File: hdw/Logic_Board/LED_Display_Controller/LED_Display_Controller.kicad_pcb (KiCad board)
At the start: 4 copper layers, 855 parts, among them J1101 USB_B_Mini, J1401 Encoder Ext, J1601 POS5P EXT, J1602 POS5P PGOOD, J1603 POS5P_THWN, J1604 POS5P_RUN, J201 +12V IN, J202 GND IN, J203 +12V IN AUX, J204 Master Power SW, J2901 STRING 1, J2902 STRING 2, J2903 STRING 3, J2904 STRING 4, J3001 USB UART, J3002 WIFI UART, J3003 FLASH SPI, J3004 Panel TP, J501 PICKIT3, J901 ESP8266 Socket, Q201 IPC100N04S51R7ATMA1, Q202 IPC100N04S51R7ATMA1, Q501 BSS214NW, Q901 BSS214NW, SW1401 Display Enable, SW1402 Brightness/Enable, SW501 MRST, U1001 ISO7321C, U1101 LT6700-1-S6, U1102 FT234XD, U1103 74LVC1G06, U1104 TPD3S014DBVR, U1201 74LVC1G06, U1202 74LVC1G06, U1203 74LVC1G06, U1204 74LVC1G06, U1205 74LVC1G06, U1206 74LVC1G06, U1207 74LVC1G06, U1301 74LVC1G06, U1302 74LVC1G06, U1303 74LVC1G06, U1304 74LVC1G06, U1401 MAX6816, U1402 74LVC2G14, U1403 74LVC1G79, U1601 LM1117-ADJ, U1602 NUP2202, U1603 74LVC1G17, U1604 74LVC1G17, U1605 74LVC1G17, U1606 NUP2202, U1701 CY7C1010DV33, U1801 SST25PF020B, U1901 SST25PF020B, U2001 SST25PF020B, U201 LTC4365DDB, U2101 SST25PF020B, U2201 SST25PF020B, U2301 SST25PF020B, U2401 SST25PF020B, U2501 SST25PF020B, U2601 74HCT541, U2602 74HCT541, U2701 74HCT541, U2702 74HCT541, U2801 74LVC1G32, U2802 74HCT541, U301 LTC3605A_UF, U401 LTC3624DD, U601 PIC32MZ2048EFH144_IPL

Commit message: Arranged USB, routed EBI
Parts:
- removed the C1801 at (123.3, 175.6)
- removed the C1801 at (123.3, 168.6)
- removed the C1801 at (123.3, 161.6)
- removed the C1801 at (123.3, 154.6)
- removed the C1801 at (123.3, 147.6)
- removed the C1801 at (123.3, 140.6)
- removed the C1801 at (123.3, 133.6)
- removed the C1802 at (123.3, 177.0)
- removed the C1802 at (123.3, 170.0)
- removed the C1802 at (123.3, 163.0)
- removed the C1802 at (123.3, 156.0)
- removed the C1802 at (123.3, 149.0)
- removed the C1802 at (123.3, 142.0)
- removed the C1802 at (123.3, 135.0)
- removed the C1803 at (123.3, 178.4)
- removed the C1803 at (123.3, 171.4)
- removed the C1803 at (123.3, 164.4)
- removed the C1803 at (123.3, 157.4)
- removed the C1803 at (123.3, 150.4)
- removed the C1803 at (123.3, 143.4)
- removed the C1803 at (123.3, 136.4)
- removed the R1801 at (130.3, 179.0)
- removed the R1801 at (130.3, 172.0)
- removed the R1801 at (130.3, 165.0)
- removed the R1801 at (130.3, 158.0)
- removed the R1801 at (130.3, 151.0)
- removed the R1801 at (130.3, 144.0)
- removed the R1801 at (130.3, 137.0)
- removed the R1802 at (130.3, 176.3)
- removed the R1802 at (130.3, 169.3)
- removed the R1802 at (130.3, 162.3)
- removed the R1802 at (130.3, 155.3)
- removed the R1802 at (130.3, 148.3)
- removed the R1802 at (130.3, 141.3)
- removed the R1802 at (130.3, 134.3)
- removed the R1803 at (116.3, 177.8)
- removed the R1803 at (116.3, 170.8)
- removed the R1803 at (116.3, 163.8)
- removed the R1803 at (116.3, 156.8)
- removed the R1803 at (116.3, 149.8)
- removed the R1803 at (116.3, 142.8)
- removed the R1803 at (116.3, 135.8)
- removed the R1804 at (116.3, 175.0)
- removed the R1804 at (116.3, 168.0)
- removed the R1804 at (116.3, 161.0)
- removed the R1804 at (116.3, 154.0)
- removed the R1804 at (116.3, 147.0)
- removed the R1804 at (116.3, 140.0)
- removed the R1804 at (116.3, 133.0)
- removed the R1805 at (130.3, 177.7)
- removed the R1805 at (130.3, 170.7)
- removed the R1805 at (130.3, 163.7)
- removed the R1805 at (130.3, 156.7)
- removed the R1805 at (130.3, 149.7)
- removed the R1805 at (130.3, 142.7)
- removed the R1805 at (130.3, 135.7)
- removed the R1806 at (116.3, 177.8)
- removed the R1806 at (116.3, 170.8)
- removed the R1806 at (116.3, 163.8)
- removed the R1806 at (116.3, 156.8)
- removed the R1806 at (116.3, 149.8)
- removed the R1806 at (116.3, 142.8)
- removed the R1806 at (116.3, 135.8)
- removed the R1807 at (116.3, 175.0)
- removed the R1807 at (116.3, 168.0)
- removed the R1807 at (116.3, 161.0)
- removed the R1807 at (116.3, 154.0)
- removed the R1807 at (116.3, 147.0)
- removed the R1807 at (116.3, 140.0)
- removed the R1807 at (116.3, 133.0)
- removed the R1808 at (130.3, 177.7)
- removed the R1808 at (130.3, 170.7)
- removed the R1808 at (130.3, 163.7)
- removed the R1808 at (130.3, 156.7)
- removed the R1808 at (130.3, 149.7)
- removed the R1808 at (130.3, 142.7)
- removed the R1808 at (130.3, 135.7)
- removed the R1809 at (130.3, 176.3)
- removed the R1809 at (130.3, 169.3)
- removed the R1809 at (130.3, 162.3)
- removed the R1809 at (130.3, 155.3)
- removed the R1809 at (130.3, 148.3)
- removed the R1809 at (130.3, 141.3)
- removed the R1809 at (130.3, 134.3)
- removed the R1810 at (130.3, 179.0)
- removed the R1810 at (130.3, 172.0)
- removed the R1810 at (130.3, 165.0)
- removed the R1810 at (130.3, 158.0)
- removed the R1810 at (130.3, 151.0)
- removed the R1810 at (130.3, 144.0)
- removed the R1810 at (130.3, 137.0)
- removed the R1811 at (116.3, 176.4)
- removed the R1811 at (116.3, 169.4)
- removed the R1811 at (116.3, 162.4)
- removed the R1811 at (116.3, 155.4)
- removed the R1811 at (116.3, 148.4)
- removed the R1811 at (116.3, 141.4)
- removed the R1811 at (116.3, 134.4)
- removed the R1812 at (116.3, 176.4)
- removed the R1812 at (116.3, 169.4)
- removed the R1812 at (116.3, 162.4)
- removed the R1812 at (116.3, 155.4)
- removed the R1812 at (116.3, 148.4)
- removed the R1812 at (116.3, 141.4)
- removed the R1812 at (116.3, 134.4)
- removed the R2601 at (121.8, 93.4)
- removed the R2601 at (121.8, 78.4)
- removed the R2601 at (121.8, 63.4)
- removed the R2601 at (121.8, 48.4)
- removed the R2602 at (121.8, 94.8)
- removed the R2602 at (121.8, 79.8)
- removed the R2602 at (121.8, 64.8)
- removed the R2602 at (121.8, 49.8)
- removed the R2603 at (121.8, 96.2)
- removed the R2603 at (121.8, 81.2)
- removed the R2603 at (121.8, 66.2)
- removed the R2603 at (121.8, 51.2)
- removed the R2604 at (121.8, 97.6)
- removed the R2604 at (121.8, 82.6)
- removed the R2604 at (121.8, 67.6)
- removed the R2604 at (121.8, 52.6)
- removed the R2605 at (121.8, 99.0)
- removed the R2605 at (121.8, 84.0)
- removed the R2605 at (121.8, 69.0)
- removed the R2605 at (121.8, 54.0)
- removed the R2606 at (121.8, 100.4)
- removed the R2606 at (121.8, 85.4)
- removed the R2606 at (121.8, 70.4)
- removed the R2606 at (121.8, 55.4)
- removed the R2615 at (121.8, 93.4)
- removed the R2615 at (121.8, 78.4)
- removed the R2615 at (121.8, 63.4)
- removed the R2615 at (121.8, 48.4)
- removed the R2617 at (121.8, 94.8)
- removed the R2617 at (121.8, 79.8)
- removed the R2617 at (121.8, 64.8)
- removed the R2617 at (121.8, 49.8)
- removed the R2619 at (121.8, 96.2)
- removed the R2619 at (121.8, 81.2)
- removed the R2619 at (121.8, 66.2)
- removed the R2619 at (121.8, 51.2)
- removed the R2621 at (121.8, 97.6)
- removed the R2621 at (121.8, 82.6)
- removed the R2621 at (121.8, 67.6)
- removed the R2621 at (121.8, 52.6)
- removed the R2623 at (121.8, 99.0)
- removed the R2623 at (121.8, 84.0)
- removed the R2623 at (121.8, 69.0)
- removed the R2623 at (121.8, 54.0)
- removed the R2625 at (121.8, 100.4)
- removed the R2625 at (121.8, 85.4)
- removed the R2625 at (121.8, 70.4)
- removed the R2625 at (121.8, 55.4)
- removed the R2627 at (121.8, 101.8)
- removed the R2627 at (121.8, 86.8)
- removed the R2627 at (121.8, 71.8)
- removed the R2627 at (121.8, 56.8)
- removed the R2629 at (121.8, 103.2)
- removed the R2629 at (121.8, 88.2)
- removed the R2629 at (121.8, 73.2)
- removed the R2629 at (121.8, 58.2)
- removed the R2631 at (136.0, 94.8)
- removed the R2631 at (136.0, 79.8)
- removed the R2631 at (136.0, 64.8)
- removed the R2631 at (136.0, 49.8)
- removed the R2633 at (136.0, 96.2)
- removed the R2633 at (136.0, 81.2)
- removed the R2633 at (136.0, 66.2)
- removed the R2633 at (136.0, 51.2)
- removed the R2635 at (136.0, 97.6)
- removed the R2635 at (136.0, 82.6)
- removed the R2635 at (136.0, 67.6)
- removed the R2635 at (136.0, 52.6)
- removed the R2637 at (136.0, 99.0)
- removed the R2637 at (136.0, 84.0)
- removed the R2637 at (136.0, 69.0)
- removed the R2637 at (136.0, 54.0)
- removed the R2639 at (136.0, 100.4)
- removed the R2639 at (136.0, 85.4)
- removed the R2639 at (136.0, 70.4)
- removed the R2639 at (136.0, 55.4)
- removed the R2641 at (136.0, 101.8)
- removed the R2641 at (136.0, 86.8)
- removed the R2641 at (136.0, 71.8)
- removed the R2641 at (136.0, 56.8)
- removed the R2643 at (136.0, 94.8)
- removed the R2643 at (136.0, 79.8)
- removed the R2643 at (136.0, 64.8)
- removed the R2643 at (136.0, 49.8)
- removed the R2644 at (136.0, 96.2)
- removed the R2644 at (136.0, 81.2)
- removed the R2644 at (136.0, 66.2)
- removed the R2644 at (136.0, 51.2)
- removed the R2645 at (136.0, 97.6)
- removed the R2645 at (136.0, 82.6)
- removed the R2645 at (136.0, 67.6)
- removed the R2645 at (136.0, 52.6)
- removed the R2646 at (136.0, 99.0)
- removed the R2646 at (136.0, 84.0)
- removed the R2646 at (136.0, 69.0)
- removed the R2646 at (136.0, 54.0)
- removed the R2647 at (136.0, 100.4)
- removed the R2647 at (136.0, 85.4)
- removed the R2647 at (136.0, 70.4)
- removed the R2647 at (136.0, 55.4)
- removed the R2648 at (136.0, 101.8)
- removed the R2648 at (136.0, 86.8)
- removed the R2648 at (136.0, 71.8)
- removed the R2648 at (136.0, 56.8)
- removed the U1801 at (123.3, 177.0)
- removed the U1801 at (123.3, 170.0)
- removed the U1801 at (123.3, 163.0)
- removed the U1801 at (123.3, 156.0)
- removed the U1801 at (123.3, 149.0)
- removed the U1801 at (123.3, 142.0)
- removed the U1801 at (123.3, 135.0)
- added C1801: 0.1uF, Capacitors_SMD:C_0603, B.Cu at (123.3, 182.6)
- added C1801: 0.1uF, Capacitors_SMD:C_0603, B.Cu at (123.3, 174.6)
- added C1801: 0.1uF, Capacitors_SMD:C_0603, B.Cu at (123.3, 166.6)
- added C1801: 0.1uF, Capacitors_SMD:C_0603, B.Cu at (123.3, 158.6)
- added C1801: 0.1uF, Capacitors_SMD:C_0603, B.Cu at (123.3, 150.6)
- added C1801: 0.1uF, Capacitors_SMD:C_0603, B.Cu at (123.3, 142.6)
- added C1801: 0.1uF, Capacitors_SMD:C_0603, B.Cu at (123.3, 134.6)
- added C1802: 10nF, Capacitors_SMD:C_0603, B.Cu at (123.3, 184.0)
- added C1802: 10nF, Capacitors_SMD:C_0603, B.Cu at (123.3, 176.0)
- added C1802: 10nF, Capacitors_SMD:C_0603, B.Cu at (123.3, 168.0)
- added C1802: 10nF, Capacitors_SMD:C_0603, B.Cu at (123.3, 160.0)
- added C1802: 10nF, Capacitors_SMD:C_0603, B.Cu at (123.3, 152.0)
- added C1802: 10nF, Capacitors_SMD:C_0603, B.Cu at (123.3, 144.0)
- added C1802: 10nF, Capacitors_SMD:C_0603, B.Cu at (123.3, 136.0)
- added C1803: 1nF, Capacitors_SMD:C_0603, B.Cu at (123.3, 185.4)
- added C1803: 1nF, Capacitors_SMD:C_0603, B.Cu at (123.3, 177.4)
- added C1803: 1nF, Capacitors_SMD:C_0603, B.Cu at (123.3, 169.4)
- added C1803: 1nF, Capacitors_SMD:C_0603, B.Cu at (123.3, 161.4)
- added C1803: 1nF, Capacitors_SMD:C_0603, B.Cu at (123.3, 153.4)
- added C1803: 1nF, Capacitors_SMD:C_0603, B.Cu at (123.3, 145.4)
- added C1803: 1nF, Capacitors_SMD:C_0603, B.Cu at (123.3, 137.4)
- added R1801: 100, Resistors_SMD:R_0603, F.Cu at (130.3, 186.2)
- added R1801: 100, Resistors_SMD:R_0603, F.Cu at (130.3, 178.2)
- added R1801: 100, Resistors_SMD:R_0603, F.Cu at (130.3, 170.2)
- added R1801: 100, Resistors_SMD:R_0603, F.Cu at (130.3, 162.2)
- added R1801: 100, Resistors_SMD:R_0603, F.Cu at (130.3, 154.2)
- added R1801: 100, Resistors_SMD:R_0603, F.Cu at (130.3, 146.2)
- added R1801: 100, Resistors_SMD:R_0603, F.Cu at (130.3, 138.2)
- added R1802: 100, Resistors_SMD:R_0603, F.Cu at (130.3, 183.1)
- added R1802: 100, Resistors_SMD:R_0603, F.Cu at (130.3, 175.1)
- added R1802: 100, Resistors_SMD:R_0603, F.Cu at (130.3, 167.1)
- added R1802: 100, Resistors_SMD:R_0603, F.Cu at (130.3, 159.1)
- added R1802: 100, Resistors_SMD:R_0603, F.Cu at (130.3, 151.1)
- added R1802: 100, Resistors_SMD:R_0603, F.Cu at (130.3, 143.1)
- added R1802: 100, Resistors_SMD:R_0603, F.Cu at (130.3, 135.1)
- added R1803: 100, Resistors_SMD:R_0603, F.Cu at (116.3, 184.9)
- added R1803: 100, Resistors_SMD:R_0603, F.Cu at (116.3, 176.9)
- added R1803: 100, Resistors_SMD:R_0603, F.Cu at (116.3, 168.9)
- added R1803: 100, Resistors_SMD:R_0603, F.Cu at (116.3, 160.9)
- added R1803: 100, Resistors_SMD:R_0603, F.Cu at (116.3, 152.9)
- added R1803: 100, Resistors_SMD:R_0603, F.Cu at (116.3, 144.9)
- added R1803: 100, Resistors_SMD:R_0603, F.Cu at (116.3, 136.9)
- added R1804: 100, Resistors_SMD:R_0603, F.Cu at (116.3, 181.9)
- added R1804: 100, Resistors_SMD:R_0603, F.Cu at (116.3, 173.9)
- added R1804: 100, Resistors_SMD:R_0603, F.Cu at (116.3, 165.9)
- added R1804: 100, Resistors_SMD:R_0603, F.Cu at (116.3, 157.9)
- added R1804: 100, Resistors_SMD:R_0603, F.Cu at (116.3, 149.9)
- added R1804: 100, Resistors_SMD:R_0603, F.Cu at (116.3, 141.9)
- added R1804: 100, Resistors_SMD:R_0603, F.Cu at (116.3, 133.9)
- added R1805: 100, Resistors_SMD:R_0603, F.Cu at (130.3, 184.7)
- added R1805: 100, Resistors_SMD:R_0603, F.Cu at (130.3, 176.7)
- added R1805: 100, Resistors_SMD:R_0603, F.Cu at (130.3, 168.7)
- added R1805: 100, Resistors_SMD:R_0603, F.Cu at (130.3, 160.7)
- added R1805: 100, Resistors_SMD:R_0603, F.Cu at (130.3, 152.7)
- added R1805: 100, Resistors_SMD:R_0603, F.Cu at (130.3, 144.7)
- added R1805: 100, Resistors_SMD:R_0603, F.Cu at (130.3, 136.7)
- added R1806: 10k, Resistors_SMD:R_0603, B.Cu at (116.3, 184.9)
- added R1806: 10k, Resistors_SMD:R_0603, B.Cu at (116.3, 176.9)
- added R1806: 10k, Resistors_SMD:R_0603, B.Cu at (116.3, 168.9)
- added R1806: 10k, Resistors_SMD:R_0603, B.Cu at (116.3, 160.9)
- added R1806: 10k, Resistors_SMD:R_0603, B.Cu at (116.3, 152.9)
- added R1806: 10k, Resistors_SMD:R_0603, B.Cu at (116.3, 144.9)
- added R1806: 10k, Resistors_SMD:R_0603, B.Cu at (116.3, 136.9)
- added R1807: 10k, Resistors_SMD:R_0603, B.Cu at (116.3, 181.9)
- added R1807: 10k, Resistors_SMD:R_0603, B.Cu at (116.3, 173.9)
- added R1807: 10k, Resistors_SMD:R_0603, B.Cu at (116.3, 165.9)
- added R1807: 10k, Resistors_SMD:R_0603, B.Cu at (116.3, 157.9)
- added R1807: 10k, Resistors_SMD:R_0603, B.Cu at (116.3, 149.9)
- added R1807: 10k, Resistors_SMD:R_0603, B.Cu at (116.3, 141.9)
- added R1807: 10k, Resistors_SMD:R_0603, B.Cu at (116.3, 133.9)
- added R1808: 10k, Resistors_SMD:R_0603, B.Cu at (130.3, 184.7)
- added R1808: 10k, Resistors_SMD:R_0603, B.Cu at (130.3, 176.7)
- added R1808: 10k, Resistors_SMD:R_0603, B.Cu at (130.3, 168.7)
- added R1808: 10k, Resistors_SMD:R_0603, B.Cu at (130.3, 160.7)
- added R1808: 10k, Resistors_SMD:R_0603, B.Cu at (130.3, 152.7)
- added R1808: 10k, Resistors_SMD:R_0603, B.Cu at (130.3, 144.7)
- added R1808: 10k, Resistors_SMD:R_0603, B.Cu at (130.3, 136.7)
- added R1809: 10k, Resistors_SMD:R_0603, B.Cu at (130.3, 183.1)
- added R1809: 10k, Resistors_SMD:R_0603, B.Cu at (130.3, 175.1)
- added R1809: 10k, Resistors_SMD:R_0603, B.Cu at (130.3, 167.1)
- added R1809: 10k, Resistors_SMD:R_0603, B.Cu at (130.3, 159.1)
- added R1809: 10k, Resistors_SMD:R_0603, B.Cu at (130.3, 151.1)
- added R1809: 10k, Resistors_SMD:R_0603, B.Cu at (130.3, 143.1)
- added R1809: 10k, Resistors_SMD:R_0603, B.Cu at (130.3, 135.1)
- added R1810: 10k, Resistors_SMD:R_0603, B.Cu at (130.3, 186.2)
- added R1810: 10k, Resistors_SMD:R_0603, B.Cu at (130.3, 178.2)
- added R1810: 10k, Resistors_SMD:R_0603, B.Cu at (130.3, 170.2)
- added R1810: 10k, Resistors_SMD:R_0603, B.Cu at (130.3, 162.2)
- added R1810: 10k, Resistors_SMD:R_0603, B.Cu at (130.3, 154.2)
- added R1810: 10k, Resistors_SMD:R_0603, B.Cu at (130.3, 146.2)
- added R1810: 10k, Resistors_SMD:R_0603, B.Cu at (130.3, 138.2)
- added R1811: 10k, Resistors_SMD:R_0603, B.Cu at (116.3, 183.4)
- added R1811: 10k, Resistors_SMD:R_0603, B.Cu at (116.3, 175.4)
- added R1811: 10k, Resistors_SMD:R_0603, B.Cu at (116.3, 167.4)
- added R1811: 10k, Resistors_SMD:R_0603, B.Cu at (116.3, 159.4)
- added R1811: 10k, Resistors_SMD:R_0603, B.Cu at (116.3, 151.4)
- added R1811: 10k, Resistors_SMD:R_0603, B.Cu at (116.3, 143.4)
- added R1811: 10k, Resistors_SMD:R_0603, B.Cu at (116.3, 135.4)
- added R1812: 100, Resistors_SMD:R_0603, F.Cu at (116.3, 183.4)
- added R1812: 100, Resistors_SMD:R_0603, F.Cu at (116.3, 175.4)
- added R1812: 100, Resistors_SMD:R_0603, F.Cu at (116.3, 167.4)
- added R1812: 100, Resistors_SMD:R_0603, F.Cu at (116.3, 159.4)
- added R1812: 100, Resistors_SMD:R_0603, F.Cu at (116.3, 151.4)
- added R1812: 100, Resistors_SMD:R_0603, F.Cu at (116.3, 143.4)
- added R1812: 100, Resistors_SMD:R_0603, F.Cu at (116.3, 135.4)
- added R2601: 100, Resistors_SMD:R_0603, F.Cu at (121.5, 93.0)
- added R2601: 100, Resistors_SMD:R_0603, F.Cu at (121.5, 78.0)
- added R2601: 100, Resistors_SMD:R_0603, F.Cu at (121.5, 63.0)
- added R2601: 100, Resistors_SMD:R_0603, F.Cu at (121.5, 48.0)
- added R2602: 100, Resistors_SMD:R_0603, F.Cu at (121.5, 94.5)
- added R2602: 100, Resistors_SMD:R_0603, F.Cu at (121.5, 79.5)
- added R2602: 100, Resistors_SMD:R_0603, F.Cu at (121.5, 64.5)
- added R2602: 100, Resistors_SMD:R_0603, F.Cu at (121.5, 49.5)
- added R2603: 100, Resistors_SMD:R_0603, F.Cu at (121.5, 96.1)
- added R2603: 100, Resistors_SMD:R_0603, F.Cu at (121.5, 81.1)
- added R2603: 100, Resistors_SMD:R_0603, F.Cu at (121.5, 66.1)
- added R2603: 100, Resistors_SMD:R_0603, F.Cu at (121.5, 51.1)
- added R2604: 100, Resistors_SMD:R_0603, F.Cu at (121.5, 97.6)
- added R2604: 100, Resistors_SMD:R_0603, F.Cu at (121.5, 82.6)
- added R2604: 100, Resistors_SMD:R_0603, F.Cu at (121.5, 67.6)
- added R2604: 100, Resistors_SMD:R_0603, F.Cu at (121.5, 52.6)
- added R2605: 100, Resistors_SMD:R_0603, F.Cu at (121.5, 99.1)
- added R2605: 100, Resistors_SMD:R_0603, F.Cu at (121.5, 84.1)
- added R2605: 100, Resistors_SMD:R_0603, F.Cu at (121.5, 69.1)
- added R2605: 100, Resistors_SMD:R_0603, F.Cu at (121.5, 54.1)
- added R2606: 100, Resistors_SMD:R_0603, F.Cu at (121.5, 100.6)
- added R2606: 100, Resistors_SMD:R_0603, F.Cu at (121.5, 85.6)
- added R2606: 100, Resistors_SMD:R_0603, F.Cu at (121.5, 70.6)
- added R2606: 100, Resistors_SMD:R_0603, F.Cu at (121.5, 55.6)
- added R2615: 10K, Resistors_SMD:R_0603, B.Cu at (121.5, 93.0)
- added R2615: 10K, Resistors_SMD:R_0603, B.Cu at (121.5, 78.0)
- added R2615: 10K, Resistors_SMD:R_0603, B.Cu at (121.5, 63.0)
- added R2615: 10K, Resistors_SMD:R_0603, B.Cu at (121.5, 48.0)
- added R2617: 10K, Resistors_SMD:R_0603, B.Cu at (121.5, 94.5)
- added R2617: 10K, Resistors_SMD:R_0603, B.Cu at (121.5, 79.5)
- added R2617: 10K, Resistors_SMD:R_0603, B.Cu at (121.5, 64.5)
- added R2617: 10K, Resistors_SMD:R_0603, B.Cu at (121.5, 49.5)
- added R2619: 10K, Resistors_SMD:R_0603, B.Cu at (121.5, 96.1)
- added R2619: 10K, Resistors_SMD:R_0603, B.Cu at (121.5, 81.1)
- added R2619: 10K, Resistors_SMD:R_0603, B.Cu at (121.5, 66.1)
- added R2619: 10K, Resistors_SMD:R_0603, B.Cu at (121.5, 51.1)
- added R2621: 10K, Resistors_SMD:R_0603, B.Cu at (121.5, 97.6)
- added R2621: 10K, Resistors_SMD:R_0603, B.Cu at (121.5, 82.6)
- added R2621: 10K, Resistors_SMD:R_0603, B.Cu at (121.5, 67.6)
- added R2621: 10K, Resistors_SMD:R_0603, B.Cu at (121.5, 52.6)
- added R2623: 10K, Resistors_SMD:R_0603, B.Cu at (121.5, 99.1)
- added R2623: 10K, Resistors_SMD:R_0603, B.Cu at (121.5, 84.1)
- added R2623: 10K, Resistors_SMD:R_0603, B.Cu at (121.5, 69.1)
- added R2623: 10K, Resistors_SMD:R_0603, B.Cu at (121.5, 54.1)
- added R2625: 10K, Resistors_SMD:R_0603, B.Cu at (121.5, 100.6)
- added R2625: 10K, Resistors_SMD:R_0603, B.Cu at (121.5, 85.6)
- added R2625: 10K, Resistors_SMD:R_0603, B.Cu at (121.5, 70.6)
- added R2625: 10K, Resistors_SMD:R_0603, B.Cu at (121.5, 55.6)
- added R2627: 10K, Resistors_SMD:R_0603, B.Cu at (121.5, 102.2)
- added R2627: 10K, Resistors_SMD:R_0603, B.Cu at (121.5, 87.2)
- added R2627: 10K, Resistors_SMD:R_0603, B.Cu at (121.5, 72.2)
- added R2627: 10K, Resistors_SMD:R_0603, B.Cu at (121.5, 57.2)
- added R2629: 10K, Resistors_SMD:R_0603, B.Cu at (121.5, 103.7)
- added R2629: 10K, Resistors_SMD:R_0603, B.Cu at (121.5, 88.7)
- added R2629: 10K, Resistors_SMD:R_0603, B.Cu at (121.5, 73.7)
- added R2629: 10K, Resistors_SMD:R_0603, B.Cu at (121.5, 58.7)
- added R2631: 10K, Resistors_SMD:R_0603, B.Cu at (136.3, 102.0)
- added R2631: 10K, Resistors_SMD:R_0603, B.Cu at (136.3, 87.0)
- added R2631: 10K, Resistors_SMD:R_0603, B.Cu at (136.3, 72.0)
- added R2631: 10K, Resistors_SMD:R_0603, B.Cu at (136.3, 57.0)
- added R2633: 10K, Resistors_SMD:R_0603, B.Cu at (136.3, 100.5)
- added R2633: 10K, Resistors_SMD:R_0603, B.Cu at (136.3, 85.5)
- added R2633: 10K, Resistors_SMD:R_0603, B.Cu at (136.3, 70.5)
- added R2633: 10K, Resistors_SMD:R_0603, B.Cu at (136.3, 55.5)
- added R2635: 10K, Resistors_SMD:R_0603, B.Cu at (136.3, 99.0)
- added R2635: 10K, Resistors_SMD:R_0603, B.Cu at (136.3, 84.0)
- added R2635: 10K, Resistors_SMD:R_0603, B.Cu at (136.3, 69.0)
- added R2635: 10K, Resistors_SMD:R_0603, B.Cu at (136.3, 54.0)
- added R2637: 10K, Resistors_SMD:R_0603, B.Cu at (136.3, 97.5)
- added R2637: 10K, Resistors_SMD:R_0603, B.Cu at (136.3, 82.5)
- added R2637: 10K, Resistors_SMD:R_0603, B.Cu at (136.3, 67.5)
- added R2637: 10K, Resistors_SMD:R_0603, B.Cu at (136.3, 52.5)
- added R2639: 10K, Resistors_SMD:R_0603, B.Cu at (136.3, 95.9)
- added R2639: 10K, Resistors_SMD:R_0603, B.Cu at (136.3, 80.9)
- added R2639: 10K, Resistors_SMD:R_0603, B.Cu at (136.3, 65.9)
- added R2639: 10K, Resistors_SMD:R_0603, B.Cu at (136.3, 50.9)
- added R2641: 10K, Resistors_SMD:R_0603, B.Cu at (136.3, 94.4)
- added R2641: 10K, Resistors_SMD:R_0603, B.Cu at (136.3, 79.4)
- added R2641: 10K, Resistors_SMD:R_0603, B.Cu at (136.3, 64.4)
- added R2641: 10K, Resistors_SMD:R_0603, B.Cu at (136.3, 49.4)
- added R2643: 100, Resistors_SMD:R_0603, F.Cu at (136.3, 94.4)
- added R2643: 100, Resistors_SMD:R_0603, F.Cu at (136.3, 79.4)
- added R2643: 100, Resistors_SMD:R_0603, F.Cu at (136.3, 64.4)
- added R2643: 100, Resistors_SMD:R_0603, F.Cu at (136.3, 49.4)
- added R2644: 100, Resistors_SMD:R_0603, F.Cu at (136.3, 95.9)
- added R2644: 100, Resistors_SMD:R_0603, F.Cu at (136.3, 80.9)
- added R2644: 100, Resistors_SMD:R_0603, F.Cu at (136.3, 65.9)
- added R2644: 100, Resistors_SMD:R_0603, F.Cu at (136.3, 50.9)
- added R2645: 100, Resistors_SMD:R_0603, F.Cu at (136.3, 97.5)
- added R2645: 100, Resistors_SMD:R_0603, F.Cu at (136.3, 82.5)
- added R2645: 100, Resistors_SMD:R_0603, F.Cu at (136.3, 67.5)
- added R2645: 100, Resistors_SMD:R_0603, F.Cu at (136.3, 52.5)
- added R2646: 100, Resistors_SMD:R_0603, F.Cu at (136.3, 99.0)
- added R2646: 100, Resistors_SMD:R_0603, F.Cu at (136.3, 84.0)
- added R2646: 100, Resistors_SMD:R_0603, F.Cu at (136.3, 69.0)
- added R2646: 100, Resistors_SMD:R_0603, F.Cu at (136.3, 54.0)
- added R2647: 100, Resistors_SMD:R_0603, F.Cu at (136.3, 100.5)
- added R2647: 100, Resistors_SMD:R_0603, F.Cu at (136.3, 85.5)
- added R2647: 100, Resistors_SMD:R_0603, F.Cu at (136.3, 70.5)
- added R2647: 100, Resistors_SMD:R_0603, F.Cu at (136.3, 55.5)
- added R2648: 100, Resistors_SMD:R_0603, F.Cu at (136.3, 102.0)
- added R2648: 100, Resistors_SMD:R_0603, F.Cu at (136.3, 87.0)
- added R2648: 100, Resistors_SMD:R_0603, F.Cu at (136.3, 72.0)
- added R2648: 100, Resistors_SMD:R_0603, F.Cu at (136.3, 57.0)
- added U1801: SST25PF020B, Housings_SOIC:SOIC-8_3.9x4.9mm_Pitch1.27mm, F.Cu at (123.3, 184.0)
- added U1801: SST25PF020B, Housings_SOIC:SOIC-8_3.9x4.9mm_Pitch1.27mm, F.Cu at (123.3, 176.0)
- added U1801: SST25PF020B, Housings_SOIC:SOIC-8_3.9x4.9mm_Pitch1.27mm, F.Cu at (123.3, 168.0)
- added U1801: SST25PF020B, Housings_SOIC:SOIC-8_3.9x4.9mm_Pitch1.27mm, F.Cu at (123.3, 160.0)
- added U1801: SST25PF020B, Housings_SOIC:SOIC-8_3.9x4.9mm_Pitch1.27mm, F.Cu at (123.3, 152.0)
- added U1801: SST25PF020B, Housings_SOIC:SOIC-8_3.9x4.9mm_Pitch1.27mm, F.Cu at (123.3, 144.0)
- added U1801: SST25PF020B, Housings_SOIC:SOIC-8_3.9x4.9mm_Pitch1.27mm, F.Cu at (123.3, 136.0)
- C1002, C1101, C1102, C1104, C1106, C1107, C1109, C1110, R1003, R1004, R1005, R1006, R1101, R1107, R1108, U1102: moved to B.Cu
- moved D1101 215.7 mm to (318.9, 238.5), turned to 180 degrees
- moved U1103 214.8 mm to (319.0, 236.1)
- moved L1101 214.7 mm to (300.1, 237.1), turned to 180 degrees
- moved U1101 213.9 mm to (315.3, 232.7), turned to 270 degrees
- moved U1104 211.9 mm to (300.5, 232.4)
- moved C1109 210.0 mm to (306.3, 231.6), turned to 90 degrees
- moved R1008 209.3 mm to (303.7, 216.9), turned to 90 degrees
- moved U1001 208.7 mm to (304.3, 209.8), turned to 270 degrees
- moved C1102 208.6 mm to (308.7, 227.1), turned to 270 degrees
- moved R1007 206.7 mm to (305.2, 216.9), turned to 90 degrees
- moved J1101 205.7 mm to (304.4, 243.0)
- moved R1006 205.3 mm to (305.2, 216.9), turned to 90 degrees
- moved C1108 205.1 mm to (302.6, 236.0), turned to 270 degrees
- moved C1105 204.9 mm to (319.9, 232.7), turned to 90 degrees
- moved R1109 204.9 mm to (318.0, 227.2), turned to 180 degrees
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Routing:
- net EBI_A10: track 0.00 -> 103.5 mm, vias 0 -> 2
- net EBI_A17: track 0.00 -> 101.8 mm, vias 0 -> 2
- net EBI_A7: track 0.00 -> 96.4 mm
- net EBI_A4: track 0.00 -> 95.8 mm, vias 0 -> 2
- net EBI_A1: track 0.00 -> 88.2 mm, vias 0 -> 2
- net EBI_A3: track 0.00 -> 87.4 mm, vias 0 -> 2
- net EBI_A11: track 0.00 -> 73.4 mm, vias 0 -> 2
- net EBI_A13: track 0.00 -> 70.6 mm, vias 0 -> 2
- net EBI_A8: track 0.00 -> 69.3 mm, vias 0 -> 2
- net EBI_A0: track 0.00 -> 64.5 mm, vias 0 -> 2
- net EBI_A9: track 0.00 -> 61.1 mm, vias 0 -> 2
- net EBI_A16: track 0.00 -> 58.7 mm, vias 0 -> 2
- net EBI_A12: track 0.00 -> 57.3 mm, vias 0 -> 2
- net EBI_A14: track 0.00 -> 53.9 mm, vias 0 -> 2
- net ~EBI_OE: track 0.00 -> 52.3 mm, vias 0 -> 2
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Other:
- board text added: "Cool stuff to add: USB COM port settings near connector Layer count Copper MU Logo Team member names Project name Manufacturer logos KiCAD logo LED labels Connector Labels Test point labels Input voltage polarity Output data signal labels Functional block labels? ESD warning Heat warning Black and white picture of group in silkscreen?"
- board text added: "Level Shifting"
- board text added: "USB"
- board text removed: "Cool stuff to add: USB COM port settings near connector Layer count Copper MU Logo Team member names Project name Manufacturer logos KiCAD logo LED labels Connector Labels Test point labels Input voltage polarity Output data signal labels Functional block labels? ESD warning Heat warning"
- board text removed: "Level Shift"

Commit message: Placed ADC filter parts
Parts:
- moved R1510 397.1 mm to (21.7, 32.3)
- moved R1501 397.0 mm to (16.9, 31.0), turned to 180 degrees
- moved D1501 396.7 mm to (16.9, 35.6)
- moved R1509 395.2 mm to (21.7, 30.7), turned to 180 degrees
- moved D1505 394.2 mm to (21.7, 35.3)
- moved R1502 392.3 mm to (16.9, 32.5)
- moved C1501 391.5 mm to (16.9, 34.0)
- moved D1502 389.4 mm to (26.3, 35.4)
- moved C1505 389.4 mm to (21.7, 33.8)
- moved D1503 387.4 mm to (31.2, 35.3)
- moved R1503 385.7 mm to (26.3, 30.9), turned to 180 degrees
- moved R1504 385.4 mm to (26.3, 32.4)
- moved R1506 385.2 mm to (31.2, 32.3)
- moved C1502 384.6 mm to (26.3, 33.9)
- moved R1508 379.1 mm to (35.3, 32.3)
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
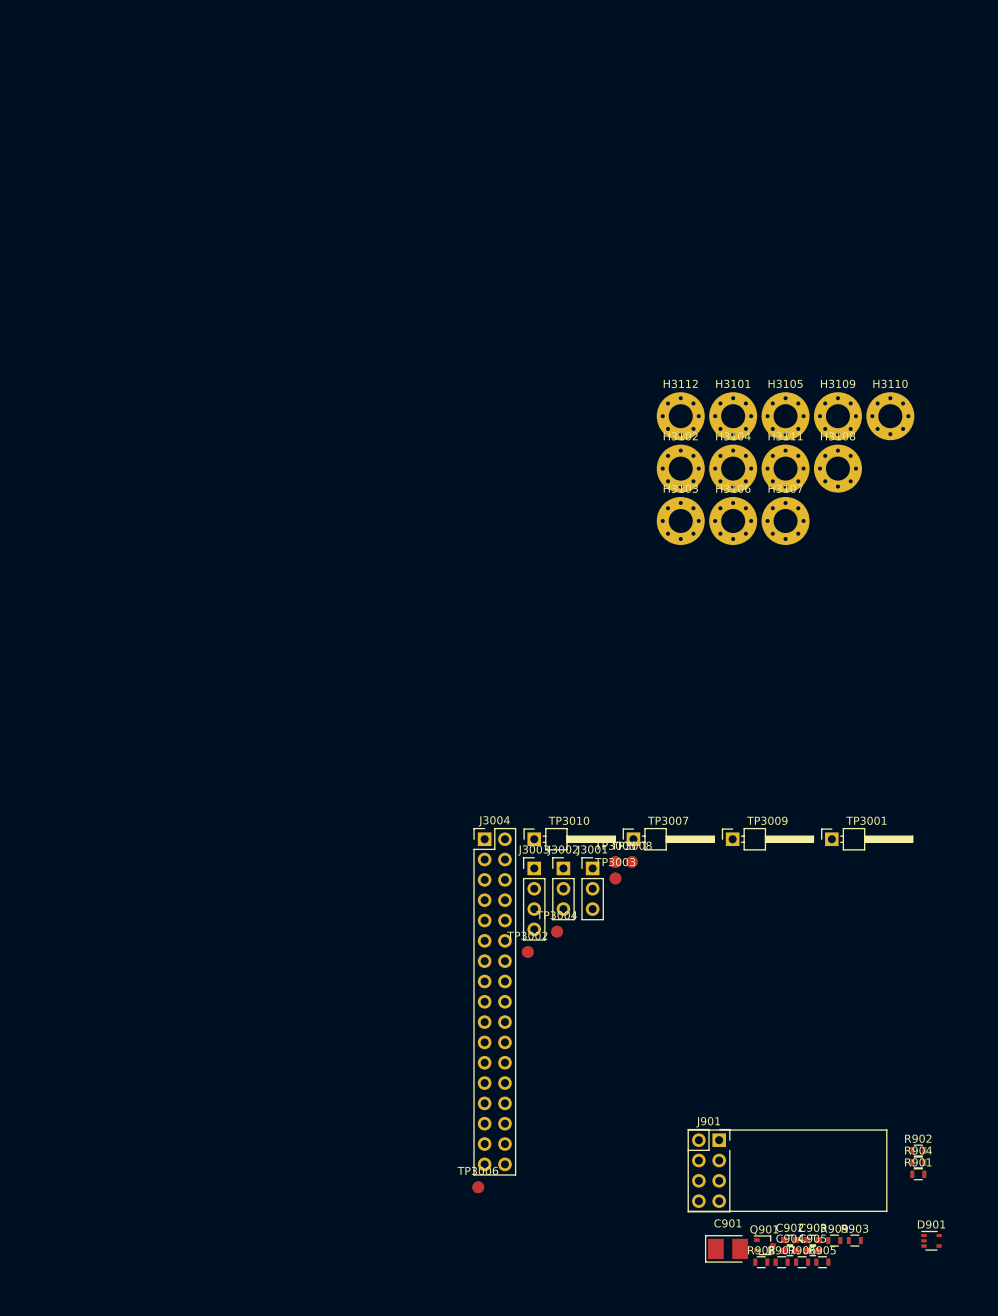
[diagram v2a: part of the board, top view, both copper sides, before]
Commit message: Resolved pinout issue with TVS diodes
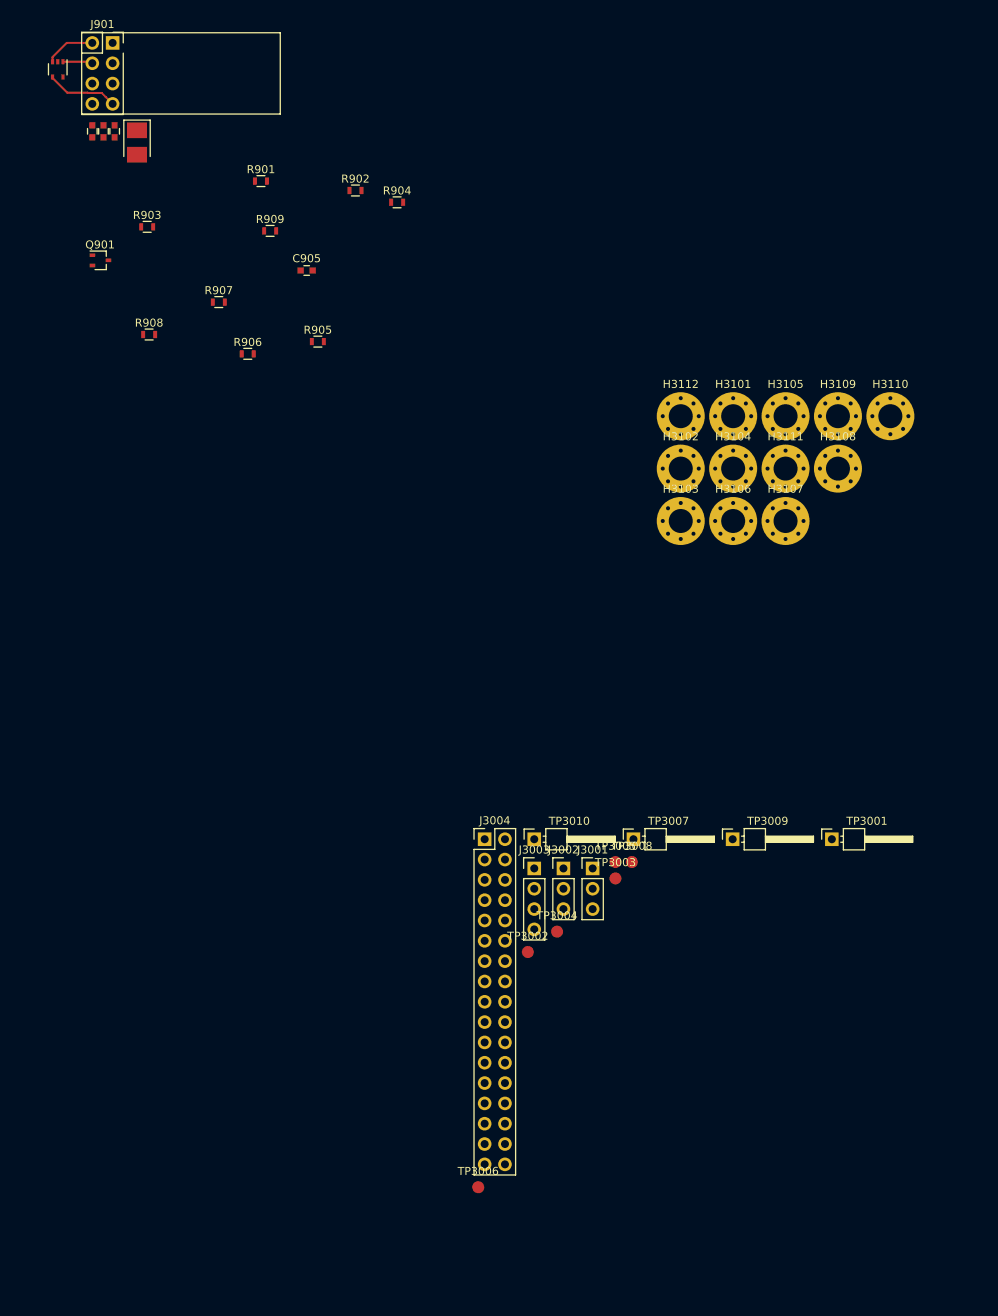
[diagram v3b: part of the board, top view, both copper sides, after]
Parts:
- moved D901 182.7 mm to (263.8, 27.8), turned to 270 degrees
- moved C904 164.9 mm to (268.1, 35.6), turned to 270 degrees
- moved C903 164.5 mm to (269.5, 35.6), turned to 270 degrees
- moved C902 162.3 mm to (270.9, 35.6), turned to 270 degrees
- moved C901 156.8 mm to (273.7, 37.0), turned to 270 degrees
- moved J901 156.7 mm to (270.6, 24.5)
- moved R903 154.5 mm to (275.0, 47.5)
- moved R901 148.9 mm to (289.2, 41.8)
- moved Q901 148.5 mm to (269.1, 51.7)
- moved R909 144.6 mm to (290.3, 48.0)
- moved R902 139.1 mm to (301.0, 43.0)
- moved R907 139.1 mm to (283.9, 56.9)
- moved R908 138.9 mm to (275.2, 61.0)
- moved C905 137.9 mm to (294.9, 53.0)
- moved R904 136.6 mm to (306.2, 44.4)
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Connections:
- D901 pad 1: Net-(D901-Pad1) -> WIFI_CHPD
- D901 pad 4: WIFI_CHPD -> Net-(D901-Pad4)
- D901 pad 5: (no net) -> Net-(C905-Pad1)
- J901 pad 7: Net-(D901-Pad1) -> Net-(D901-Pad4)
- R901 pad 2: Net-(D901-Pad1) -> Net-(D901-Pad4)
- R902 pad 2: Net-(D901-Pad1) -> Net-(D901-Pad4)
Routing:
- net Net-(D901-Pad4): track 0.00 -> 8.98 mm
- net Net-(D901-Pad3): track 0.00 -> 6.28 mm
- net WIFI_CHPD: track 0.00 -> 3.75 mm

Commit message: Cleaned up EBI a bit
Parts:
- C905, D901, R902, R903, R904, R905: moved to B.Cu
- moved R904 45.1 mm to (264.8, 26.5), turned to 180 degrees
- moved R905 45.1 mm to (264.8, 29.6)
- moved C905 39.1 mm to (264.8, 28.1), turned to 180 degrees
- moved R902 29.5 mm to (273.6, 32.1), turned to 180 degrees
- moved R903 25.1 mm to (264.8, 24.5)
- moved D901 10.1 mm to (273.8, 28.4)
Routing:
- net Net-(D901-Pad4): track 8.98 -> 0.00 mm
- net EBI_A4: track 95.8 -> 102.6 mm
- net Net-(D901-Pad3): track 6.28 -> 0.00 mm
- net EBI_A7: track 96.4 -> 101.7 mm
- net EBI_A1: track 88.2 -> 93.5 mm
- net EBI_A3: track 87.4 -> 92.6 mm
- net EBI_A10: track 103.5 -> 108.7 mm
- net EBI_A17: track 101.8 -> 107.0 mm
- net EBI_A15: track 43.3 -> 48.5 mm
- net WIFI_CHPD: track 3.75 -> 0.00 mm
- net EBI_A8: track 69.3 -> 73.0 mm
- net EBI_A9: track 61.1 -> 64.6 mm
- net EBI_A14: track 53.9 -> 56.8 mm
- net EBI_A11: track 73.4 -> 75.0 mm
- net EBI_A0: track 64.5 -> 66.1 mm
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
